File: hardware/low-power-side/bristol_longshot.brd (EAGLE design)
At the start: 36 x 44 mm, 68 parts, among them U1 SAM_D20E, U10 ADP1607ACPZN-R7, U11 TPS73118DBVT, U2 SI4060, U3 SE880, U4 SST25WF040BT-40I/NP, U5 TG-5006CJ, U6 TG-5006CJ, U7 TPS3123, U8 SN74LVC1G32DCKR, U9 MS5607-02BA03, Y1 ABS05

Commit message: [low-power-side] More work on board, vaguely complete. Added parts list
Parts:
- removed R10: 100kΩ, microbuilder_v3:_0402
- removed R11: 240kΩ, microbuilder_v3:_0402
- added R2, R3, R4: 10kΩ, microbuilder_v3:_0402
- C1, C13, C14, C15, C16, C17, C18, C19, C2, C3, C4, C5, C6, C7, C8, C9: device microbuilder_v3:_0402 -> microbuilder_v3:_0402@2
- C10: value 100nF -> 100pF; device microbuilder_v3:_0402 -> microbuilder_v3:_0402@2
- C11: value 100nF -> 1nF; device microbuilder_v3:_0402 -> microbuilder_v3:_0402@2
- C12: value 1µF -> 10nF; device microbuilder_v3:_0402 -> microbuilder_v3:_0402@2
- C20: value 18pF -> 100nF; device microbuilder_v3:_0402 -> microbuilder_v3:_0402@2
- C21: value 2.2µF -> 100nF; device microbuilder_v3:_0402 -> microbuilder_v3:_0402@2
- C22: value 4.7µF -> 100nF; device microbuilder_v3:_0402 -> microbuilder_v3:_0402@2
- C23: value 18pF -> 1µF; device microbuilder_v3:_0402 -> microbuilder_v3:_0402@2
- C24: value 1nF -> 1µF; device microbuilder_v3:_0402 -> microbuilder_v3:_0402@2
- C25: value 100nF -> 2.2µF; device microbuilder_v3:_0402 -> microbuilder_v3:_0402@2
- C26: value 10µF -> 4.7µF; device resistor:C0603K -> microbuilder_v3:_0402@2
- C27, C28: value 10µF -> 18pF; device resistor:C0603K -> microbuilder_v3:_0402@2
- C29: value 1µF -> 10µF; device microbuilder_v3:_0402 -> resistor:C0603K
- C30: value 10nF -> 10µF; device microbuilder_v3:_0402 -> resistor:C0603K
- C31: value 100µF -> 10µF; device resistor:C1210K -> resistor:C0603K
- C32: value 100pF -> 100µF; device microbuilder_v3:_0402 -> resistor:C1210K
- R7, R9: value 10kΩ -> 100kΩ
- R8: value 10kΩ -> 43kΩ
- moved C30 32.9 mm to (24.1, 39.4)
- moved C29 27.5 mm to (21.0, 39.4)
- moved C25 27.1 mm to (23.5, 12.5), turned to 0 degrees
- moved C32 24.7 mm to (23.2, 42.0), turned to 180 degrees
- moved C11 24.0 mm to (14.1, 36.2), turned to 180 degrees
- moved C24 23.6 mm to (14.2, 12.8)
- moved C20 18.2 mm to (23.5, 13.4), turned to 0 degrees
- moved C23 16.8 mm to (13.4, 13.6)
- moved R9 13.3 mm to (23.0, 36.0), turned to 180 degrees
- moved R8 11.7 mm to (21.5, 36.6)
- moved C21 10.7 mm to (12.9, 18.8), turned to 90 degrees
- moved C27 10.1 mm to (17.0, 29.5), turned to 90 degrees
- moved C31 6.90 mm to (16.6, 36.9), turned to 0 degrees
- moved C28 6.59 mm to (15.7, 30.4)
- moved R7 6.36 mm to (19.4, 25.2), turned to 0 degrees
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- renumbered U$48 to A1
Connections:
- removed net GPS!RESET: U1.4
- new net EXT_THERMISTOR_SENSE: R7.2, U1.4
- net 1.2V: now also C29.1; no longer C27.1
- net 1.8V: now also C21.1, C30.1, R4.2, R8.2; no longer C22.1, C31.1, R10.2, R7.2
- net FB: now also R8.1, R9.2; no longer R10.1, R11.2
- net GND: now also R2.1, R3.1, R7.1; no longer R11.1, R8.1
- net RADIO_VDD: now also C20.1, C25.1; no longer C11.1, C21.1
- net RTC_XI: now also C27.1; no longer C20.1
- net RTC_XO: now also C28.1; no longer C23.1
- net SE_GPIO0: now also R2.2; no longer R9.2
- net SE_GPIO1: now also R3.2; no longer R8.2
- net SE_MODE_PULL: now also R4.1; no longer R7.1
- net TCXO_REG_IN: now also C23.1; no longer C29.1
- net TCXO_REG_NR: now also C12.1; no longer C30.1
- net TCXO_VDD: now also C24.1; no longer C12.1
- net TCXO_VDD1: now also C11.1, C22.1, C31.1; no longer C24.1, C25.1, C28.1
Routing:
- net EXT_THERMISTOR_SENSE: track 0.00 -> 2.67 mm, vias 0 -> 1
- net GND: track 44.6 -> 47.2 mm, vias 88 -> 90
- net GPS_ANT: track 4.93 -> 6.93 mm
- net EXT!RESET: track 16.4 -> 17.3 mm, vias 0 -> 2
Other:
- board size 36 x 44 mm -> 38 x 44 mm
- board text added: "2.2µH"
- board text added: "680nH"
- board text added: "ADP1607"
- board text added: "Batt +"
- board text added: "Batt -"
- board text added: "Si4468"
- board text added: "TPS73118"
- board text added: "TXCO"

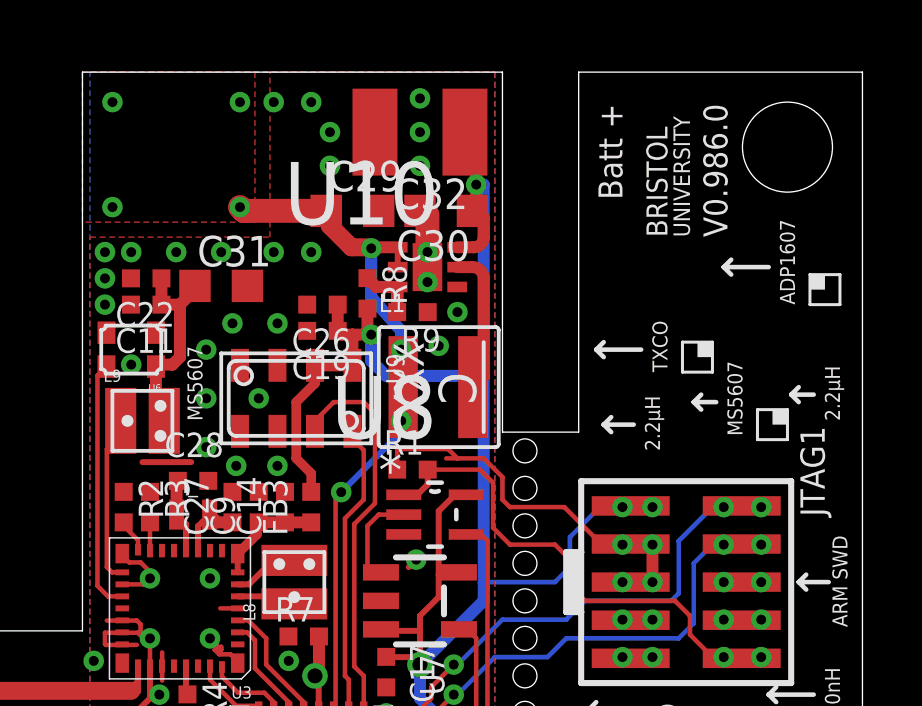
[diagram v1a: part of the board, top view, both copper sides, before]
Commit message: [low-power-side] Added 10k i2c pull ups
v0.986.0 -> v0.986.1
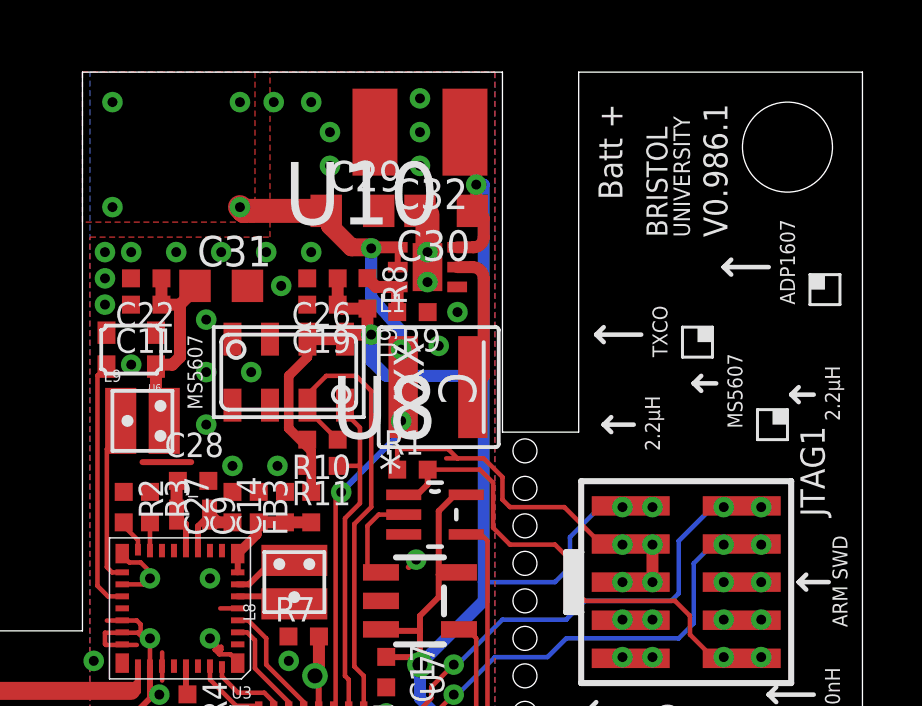
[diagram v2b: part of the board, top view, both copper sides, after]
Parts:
- added R10, R11: 10kΩ, microbuilder_v3:_0402
- moved U9 0.91 mm to (18.9, 34.0)
- moved C19 0.88 mm to (20.0, 36.2)
- moved C26 0.88 mm to (20.0, 37.1)
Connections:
- net 1.8V: now also R10.2, R11.2
- net SCL: now also R11.1
- net SDA: now also R10.1
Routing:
- net SDA: track 13.2 -> 15.6 mm
- net 1.8V: track 132.9 -> 134.8 mm
- net SCL: track 9.87 -> 11.5 mm
- net GND: vias 90 -> 89
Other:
- board text added: "V0.986.1"
- board text removed: "V0.986.0"

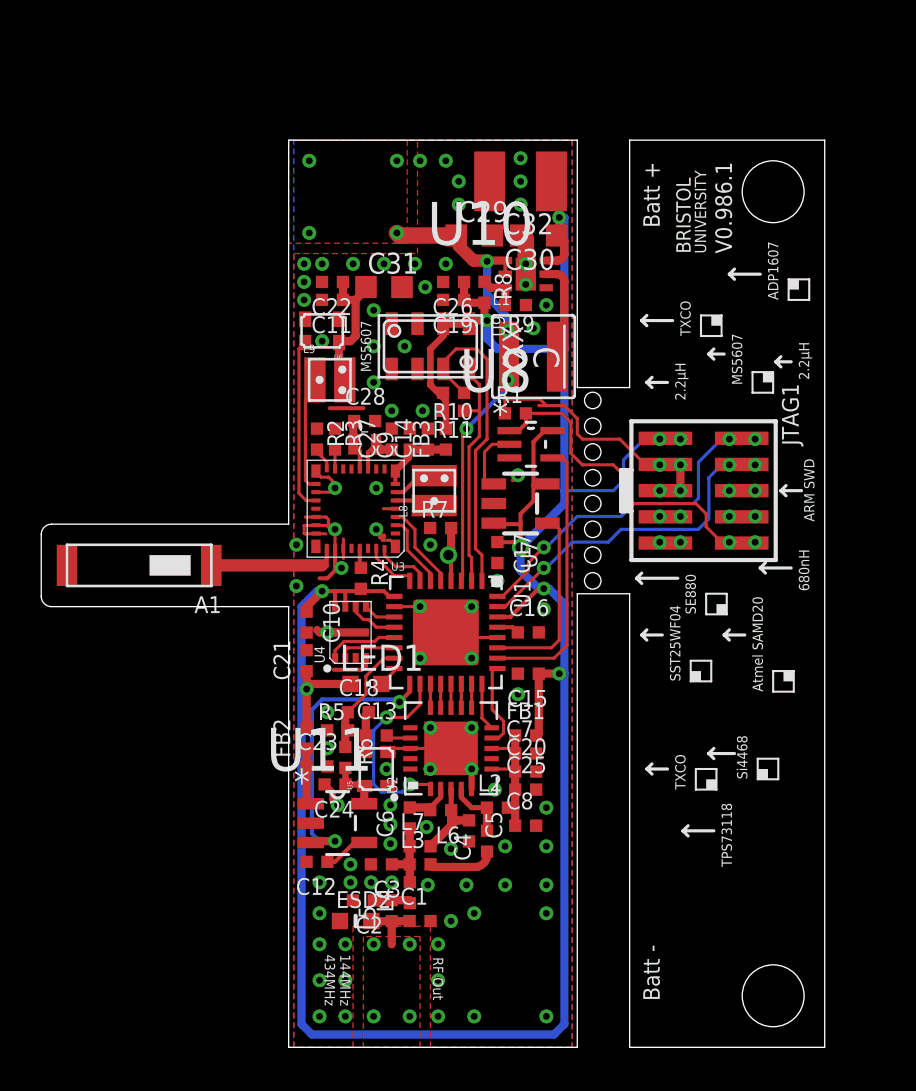
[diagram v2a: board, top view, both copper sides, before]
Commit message: [low-power] Rearranged matching section
Attempt to follow guidelines from silabs AN685 more closely
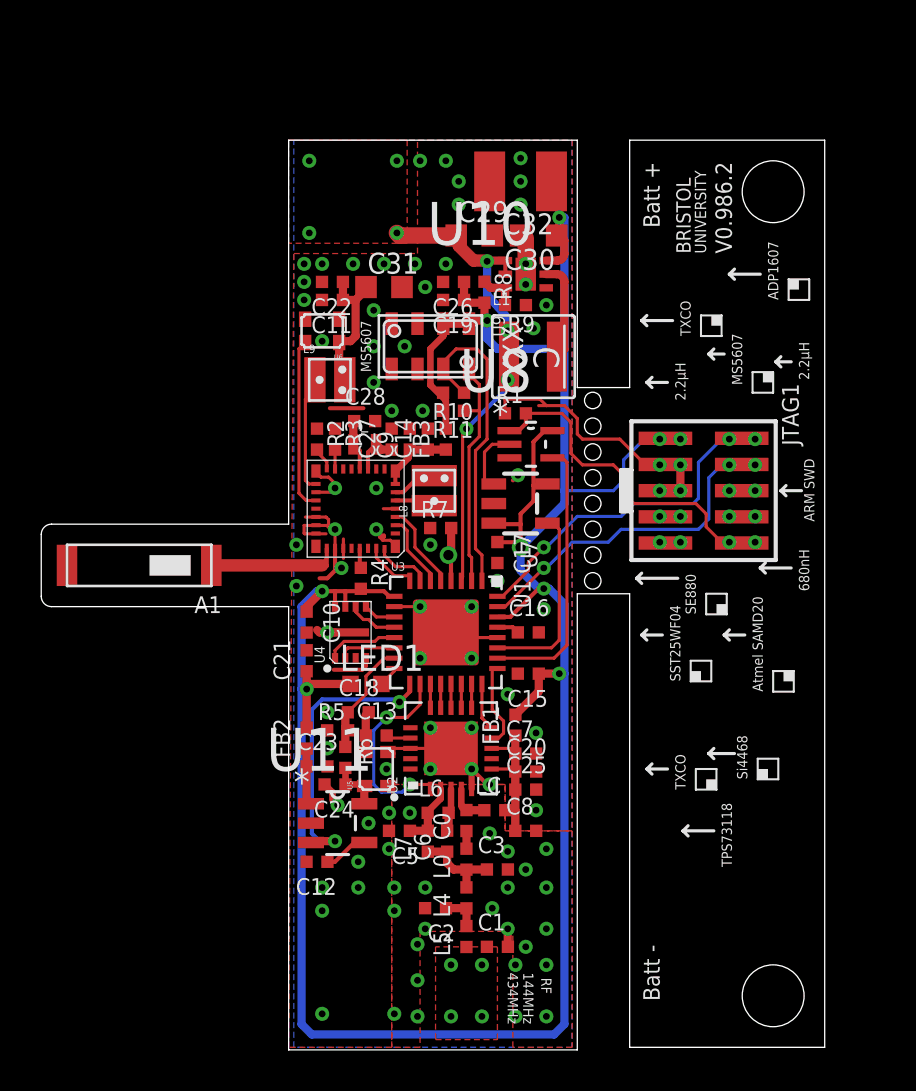
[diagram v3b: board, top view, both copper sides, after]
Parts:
- removed C4: 15pF, microbuilder_v3:_0402@2
- removed ESD2: 0.25pF, microbuilder_v3:_0603MP
- removed L2: 220nH, microbuilder_v3:_0402@1
- removed L3: 56nH, microbuilder_v3:_0402@1
- added C0: 15pF, microbuilder_v3:_0402@2
- added L0: 56nH, microbuilder_v3:_0402@1
- added LC: 220nH, microbuilder_v3:_0402@1
- moved C3 5.63 mm to (22.1, 8.62), turned to 0 degrees
- moved C1 3.95 mm to (22.1, 4.88)
- moved L5 3.83 mm to (20.6, 5.38)
- moved C2 3.52 mm to (19.1, 6.75)
- moved C5 3.38 mm to (17.4, 10.5), turned to 180 degrees
- moved L4 2.76 mm to (20.6, 7.25)
- moved C6 2.13 mm to (19.7, 10.0)
- moved FB1 0.71 mm to (23.0, 15.6), turned to 90 degrees
- moved L7 0.45 mm to (18.8, 10.0), turned to 90 degrees
- moved C8 0.25 mm to (23.5, 10.5)
- moved L6 0.18 mm to (19.2, 11.4), turned to 0 degrees
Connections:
- net ANT: no longer ESD2.2
- net FILTER1: now also L0.1; no longer L3.1
- net GND: no longer ESD2.1
- net RADIO_VDD: now also LC.2; no longer L2.2
- net RF_OUT: now also C0.2, LC.1; no longer C4.2, L2.1
- net RF_TANK: now also C0.1, L0.2; no longer C4.1, L3.2
- net RXN: now also U2.2; no longer U2.3
- net RXP: now also U2.3; no longer U2.2
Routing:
- net ANT: track 2.98 -> 0.00 mm
- net RF_TANK: track 3.20 -> 0.86 mm
- net GND: track 47.2 -> 49.3 mm, vias 89 -> 90
- net RF_OUT: track 3.24 -> 2.00 mm
- net RXN: track 4.17 -> 3.16 mm
- net FILTER1: track 3.73 -> 4.42 mm
- net 1.8V: track 134.8 -> 134.2 mm
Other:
- board size 38 x 44 mm -> 38 x 44.1 mm
- board text added: "RF"
- board text added: "V0.986.2"
- board text removed: "RF Out"
- board text removed: "V0.986.1"

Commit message: Low Power. Added L0'-C0' tank in paralell. Might work, should test
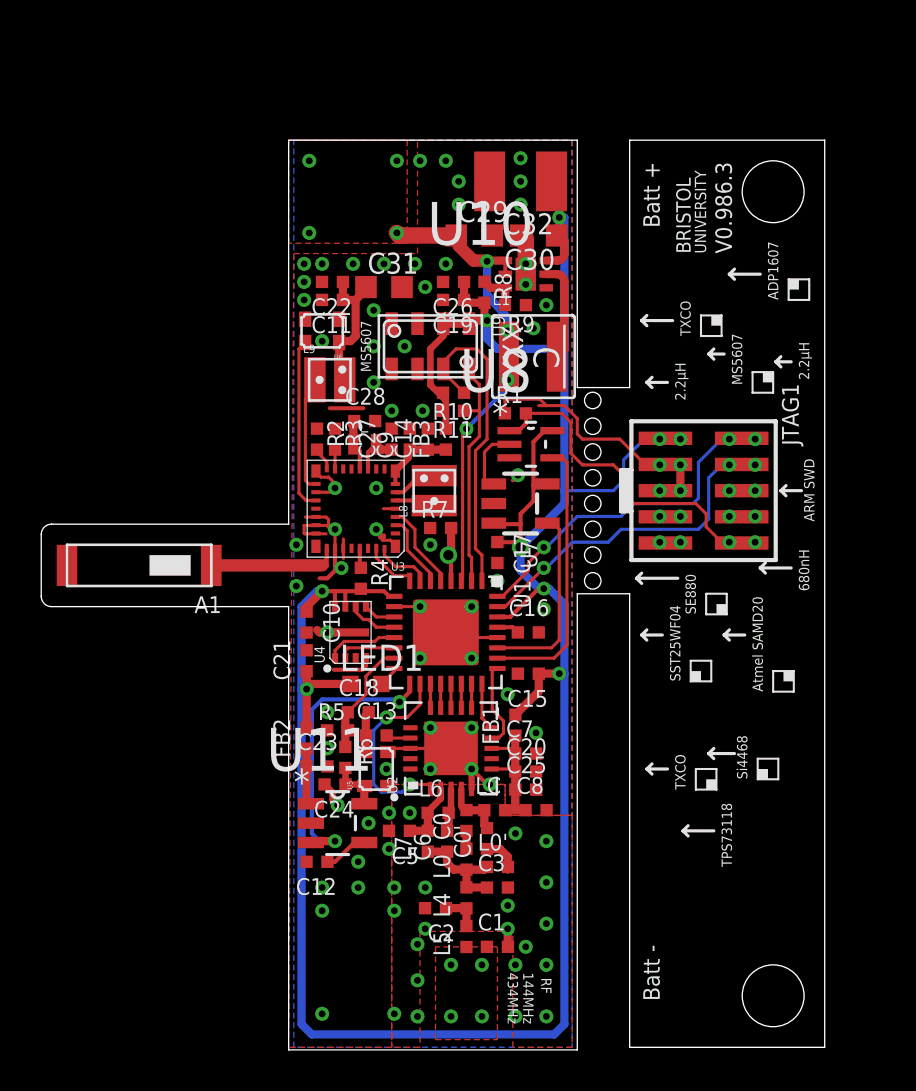
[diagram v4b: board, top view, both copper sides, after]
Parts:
- added C0': 15pF, microbuilder_v3:_0402@2
- added L0': 56nH, microbuilder_v3:_0402@1
- moved C8 1.12 mm to (24.0, 11.5)
- moved C3 0.88 mm to (22.1, 7.75)
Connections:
- new net N$5: C0'.1, L0'.2
- net FILTER1: now also L0'.1
- net RF_OUT: now also C0'.2
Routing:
- net N$5: track 0.00 -> 1.89 mm
- net FILTER1: track 4.42 -> 5.48 mm
- net RF_OUT: track 2.00 -> 2.92 mm
- net RADIO_VDD: track 8.68 -> 8.18 mm
- net GND: vias 90 -> 86
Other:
- board text added: "V0.986.3"
- board text removed: "V0.986.2"
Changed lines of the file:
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@@
 <circle x="17.125" y="12.125" radius="0.1" width="0.2" layer="21"/>
 <rectangle x1="19.125" y1="0.375" x2="22.125" y2="4.75" layer="29"/>
-<text x="33.5" y="38.5" size="0.8" layer="21" font="vector" ratio="14" rot="R90">V0.986.2</text>
+<text x="33.5" y="38.5" size="0.8" layer="21" font="vector" ratio="14" rot="R90">V0.986.3</text>
 <text x="16" y="32.75" size="0.5" layer="21" font="vector" ratio="15" rot="SR90">MS5607</text>
 <text x="35" y="17.25" size="0.5" layer="21" font="vector" ratio="15" rot="SR90">Atmel SAMD20</text>
@@
 <element name="C0" library="microbuilder_v3" package="_0402@2" value="15pF" x="20.625" y="11" rot="R90"/>
 <element name="L0" library="microbuilder_v3" package="_0402@1" value="56nH" x="20.625" y="9.125" rot="R90"/>
-<element name="C3" library="microbuilder_v3" package="_0402@2" value="8.2pF" x="22.125" y="8.625"/>
+<element name="C3" library="microbuilder_v3" package="_0402@2" value="8.2pF" x="22.125" y="7.75"/>
 <element name="L4" library="microbuilder_v3" package="_0402@1" value="18nH" x="20.625" y="7.25" rot="R90"/>
 <element name="L5" library="microbuilder_v3" package="_0402@1" value="18nH" x="20.625" y="5.375" rot="R90"/>
@@
 <element name="C25" library="microbuilder_v3" package="_0402@2" value="2.2µF" x="23.5" y="12.5"/>
 <element name="C20" library="microbuilder_v3" package="_0402@2" value="100nF" x="23.5" y="13.375"/>
-<element name="C8" library="microbuilder_v3" package="_0402@2" value="100pF" x="23.5" y="10.5"/>
+<element name="C8" library="microbuilder_v3" package="_0402@2" value="100pF" x="24" y="11.5"/>
 <element name="C7" library="microbuilder_v3" package="_0402@2" value="15pF" x="23.5" y="14.25"/>
 <element name="C9" library="microbuilder_v3" package="_0402@2" value="100pF" x="17.875" y="29.5" rot="R90"/>
@@
 <element name="R10" library="microbuilder_v3" package="_0402" value="10kΩ" x="20" y="31.75" rot="R180"/>
 <element name="R11" library="microbuilder_v3" package="_0402" value="10kΩ" x="20" y="30.875" rot="R180"/>
+<element name="L0'" library="microbuilder_v3" package="_0402@1" value="56nH" x="22.125" y="8.75"/>
+<element name="C0'" library="microbuilder_v3" package="_0402@2" value="15pF" x="21.625" y="10.125" rot="R90"/>
 </elements>
 <signals>
@@
 <vertex x="18.25" y="44"/>
 <vertex x="25.75" y="44"/>
-<vertex x="25.75" y="10.5"/>
-<vertex x="22.5" y="10.5"/>
+<vertex x="25.75" y="11.25"/>
+<vertex x="22.5" y="11.25"/>
 <vertex x="22.5" y="12.75"/>
 <vertex x="17" y="12.75"/>
@@
 <via x="23" y="1.5" extent="1-16" drill="0.3302"/>
 <via x="18.625" y="7.75" extent="1-16" drill="0.3302"/>
-<via x="21.75" y="10.375" extent="1-16" drill="0.3302"/>
 <via x="20.875" y="18.875" extent="1-16" drill="0.3302"/>
 <wire x1="19.625" y1="20.125" x2="19.625" y2="21.375" width="0.1524" layer="1"/>
@@
 <via x="17.125" y="7.75" extent="1-16" drill="0.3302"/>
 <via x="18.625" y="5.75" extent="1-16" drill="0.3302"/>
-<via x="24.5" y="9.625" extent="1-16" drill="0.3302"/>
-<via x="24" y="11.5" extent="1-16" drill="0.3302"/>
+<via x="24.5" y="10" extent="1-16" drill="0.3302"/>
 <contactref element="C14" pad="2"/>
 <contactref element="C21" pad="2"/>
@@
 <via x="18.25" y="3.25" extent="1-16" drill="0.3302"/>
 <via x="18.25" y="5" extent="1-16" drill="0.3302"/>
-<via x="22.625" y="7.75" extent="1-16" drill="0.3302"/>
-<via x="22.625" y="9.5" extent="1-16" drill="0.3302"/>
-<via x="23.5" y="8.625" extent="1-16" drill="0.3302"/>
+<via x="23" y="10.375" extent="1-16" drill="0.3302"/>
 <via x="23.5" y="4.875" extent="1-16" drill="0.3302"/>
 <via x="22.625" y="5.75" extent="1-16" drill="0.3302"/>
-<via x="24.5" y="7.75" extent="1-16" drill="0.3302"/>
-<via x="24.5" y="5.75" extent="1-16" drill="0.3302"/>
+<via x="24.5" y="8" extent="1-16" drill="0.3302"/>
+<via x="24.5" y="6" extent="1-16" drill="0.3302"/>
 <via x="24.5" y="4" extent="1-16" drill="0.3302"/>
 <via x="24.5" y="1.5" extent="1-16" drill="0.3302"/>
@@
 <vertex x="17" y="12.75"/>
 <vertex x="22.5" y="12.75"/>
-<vertex x="22.5" y="10.5"/>
-<vertex x="25.75" y="10.5"/>
+<vertex x="22.5" y="11.25"/>
+<vertex x="25.75" y="11.25"/>
 <vertex x="25.75" y="0"/>
 <vertex x="22.875" y="0"/>
@@
 <vertex x="17" y="0"/>
 </polygon>
-<via x="21.875" y="6.75" extent="1-16" drill="0.3302"/>
+<via x="22.625" y="6.875" extent="1-16" drill="0.3302"/>
 <wire x1="20.875" y1="13.5" x2="21.625" y2="12.75" width="0.2" layer="1"/>
 <wire x1="21.625" y1="12.75" x2="21.75" y2="12.75" width="0.2" layer="1"/>
@@
 <wire x1="22.992" y1="14.25" x2="22.867" y2="14.5" width="0.1524" layer="1"/>
 <wire x1="22.992" y1="12.5" x2="22.992" y2="11.5" width="0.4064" layer="1"/>
-<wire x1="22.992" y1="11.5" x2="22.992" y2="10.5" width="0.4064" layer="1"/>
 <wire x1="22.508" y1="11.5" x2="22.992" y2="11.5" width="0.4064" layer="1"/>
 <wire x1="23" y1="15.117" x2="22.992" y2="15.117" width="0.4" layer="1"/>
 <wire x1="22.992" y1="15.117" x2="22.992" y2="14.25" width="0.4" layer="1"/>
+<wire x1="22.992" y1="11.5" x2="23.492" y2="11.5" width="0.4" layer="1"/>
 </signal>
 <signal name="RF_OUT">
@@
 <wire x1="20.375" y1="12.53" x2="20.375" y2="11.758" width="0.32" layer="1"/>
 <wire x1="20.375" y1="11.758" x2="20.625" y2="11.508" width="0.32" layer="1" curve="90"/>
+<contactref element="C0'" pad="2"/>
+<wire x1="21.492" y1="11.5" x2="21.492" y2="10.766" width="0.4" layer="1"/>
+<wire x1="21.492" y1="10.766" x2="21.625" y2="10.633" width="0.4" layer="1"/>
 </signal>
 <signal name="FILTER1">
@@
 <contactref element="L7" pad="1"/>
 <contactref element="C6" pad="1"/>
-<wire x1="20.625" y1="7.758" x2="20.625" y2="8.617" width="0.4" layer="1"/>
-<wire x1="21.617" y1="8.625" x2="20.625" y2="8.625" width="0.4" layer="1"/>
 <wire x1="20.625" y1="8.625" x2="20.625" y2="8.617" width="0.4" layer="1"/>
 <wire x1="20.625" y1="8.617" x2="20.617" y2="8.625" width="0.4" layer="1"/>
@@
 <wire x1="19.6875" y1="8.9375" x2="19.6875" y2="9.492" width="0.4" layer="1"/>
 <wire x1="18.75" y1="9.492" x2="19.6875" y2="9.492" width="0.4" layer="1"/>
+<contactref element="L0'" pad="1"/>
+<wire x1="21.617" y1="7.75" x2="20.625" y2="7.75" width="0.4" layer="1"/>
+<wire x1="20.625" y1="7.75" x2="20.625" y2="7.758" width="0.4" layer="1"/>
+<wire x1="20.625" y1="8.617" x2="20.625" y2="7.758" width="0.4" layer="1"/>
+<wire x1="21.617" y1="8.75" x2="21.484" y2="8.617" width="0.4" layer="1"/>
+<wire x1="21.484" y1="8.617" x2="20.625" y2="8.617" width="0.4" layer="1"/>
 </signal>
 <signal name="FILTER2">
@@
 <wire x1="19.875" y1="23.75" x2="19.75" y2="23.875" width="0.2" layer="1"/>
 </signal>
+<signal name="N$5">
+<contactref element="L0'" pad="2"/>
+<contactref element="C0'" pad="1"/>
+<wire x1="21.625" y1="9.617" x2="22.258" y2="9.617" width="0.4" layer="1"/>
+<wire x1="22.258" y1="9.617" x2="22.625" y2="9.25" width="0.4" layer="1"/>
+<wire x1="22.625" y1="9.25" x2="22.625" y2="8.633" width="0.4" layer="1"/>
+<wire x1="22.625" y1="8.633" x2="22.633" y2="8.75" width="0.4" layer="1"/>
+</signal>
 </signals>
